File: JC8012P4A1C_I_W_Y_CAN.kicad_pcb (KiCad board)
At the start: 2 copper layers, 0 parts

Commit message: Add TBC power output, mounting holes and board outline
Schematic:
- TBC_PWR_out on D-Sub pin 8 like the Mueller-Elektronik BASIC-Terminal
  (some harnesses do not start without powered terminators):
  VIN_PROT -> SS16 Schottky (no back-feed) -> PTC 0.14 A -> J1 pin 6
- TBC_GND (D-Sub pin 3) to GND via R8 0R, DNP by default to stay
  compatible; fit R8 only if a harness needs the TBC_GND return
- Mounting holes H1-H4, M2, 2.2 mm (ISO 273 medium)
- Labels oriented away from pins, overlapping parts moved apart
  (netlist unchanged)

Board:
- Footprints imported from schematic (not placed yet)
- Outline 66 x 54 mm (provisional), holes on 58 x 46 mm grid,
  4 mm from the edge

Co-Authored-By: Claude Opus 5.5 <noreply@anthropic.com>
Claude-Session: https://claude.ai/code/session_014h8cGi8SRWthYdGFH1Qgzz
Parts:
- added C1: 47n, Capacitor_SMD:C_0603_1608Metric, F.Cu at (0.00, 0.00)
- added C2, C3: 100n, Capacitor_SMD:C_0603_1608Metric, F.Cu at (0.00, 0.00)
- added C4: 10u/50V, Capacitor_SMD:C_1210_3225Metric, F.Cu at (0.00, 0.00)
- added C5: 100u/10V, Capacitor_SMD:C_1210_3225Metric, F.Cu at (0.00, 0.00)
- added C6, C7: 22n, Capacitor_SMD:C_0603_1608Metric, F.Cu at (0.00, 0.00)
- added D1: 824094024, JC8012P4A1C_CAN:D_Wurth_WE-TVS-SOT23-3L, F.Cu at (0.00, 0.00)
- added D2: 824551241, JC8012P4A1C_CAN:D_Wurth_WE-TVSP-DO214-AB-3000W_BI, F.Cu at (0.00, 0.00)
- added D3: 15V, Diode_SMD:D_SOD-123, F.Cu at (0.00, 0.00)
- added D4: SS16, Diode_SMD:D_SMA, F.Cu at (0.00, 0.00)
- added F1: 1A slow, Fuse:Fuse_1206_3216Metric, F.Cu at (0.00, 0.00)
- added F2: PTC 0.14A/60V, Fuse:Fuse_1812_4532Metric, F.Cu at (0.00, 0.00)
- added H1: M2, MountingHole:MountingHole_2.2mm_M2, F.Cu at (104.0, 104.0)
- added H2: M2, MountingHole:MountingHole_2.2mm_M2, F.Cu at (162.0, 104.0)
- added H3: M2, MountingHole:MountingHole_2.2mm_M2, F.Cu at (104.0, 150.0)
- added H4: M2, MountingHole:MountingHole_2.2mm_M2, F.Cu at (162.0, 150.0)
- added J1: 61201022921, JC8012P4A1C_CAN:J_Wurth_WR-BHD_61201022921, F.Cu at (0.00, 0.00)
- added J2: 68711414522, JC8012P4A1C_CAN:J_Wurth_WR-FPC_68711414522, F.Cu at (0.00, 0.00)
- added J3: 653104131822, JC8012P4A1C_CAN:J_Wurth_WR-WTB_653104131822, F.Cu at (0.00, 0.00)
- added Q1: DMP6050SSD, Package_SO:SOIC-8_3.9x4.9mm_P1.27mm, F.Cu at (0.00, 0.00)
- added R1, R2: 750, Resistor_SMD:R_0603_1608Metric, F.Cu at (0.00, 0.00)
- added R3: 10k, Resistor_SMD:R_0603_1608Metric, F.Cu at (0.00, 0.00)
- added R4, R5: 100k, Resistor_SMD:R_0603_1608Metric, F.Cu at (0.00, 0.00)
- added R6: 5k62, Resistor_SMD:R_0603_1608Metric, F.Cu at (0.00, 0.00)
- added R7: 1k07, Resistor_SMD:R_0603_1608Metric, F.Cu at (0.00, 0.00)
- added R8: 0R DNP, Resistor_SMD:R_0603_1608Metric, F.Cu at (0.00, 0.00)
- added U1: TLE9250VSJ, Package_SO:SOIC-8_3.9x4.9mm_P1.27mm, F.Cu at (0.00, 0.00)
- added U2: 171030601, JC8012P4A1C_CAN:U_Wurth_WPME-VDRM-TO263-7EP, F.Cu at (0.00, 0.00)
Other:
- board outline added: 66 x 54 mm

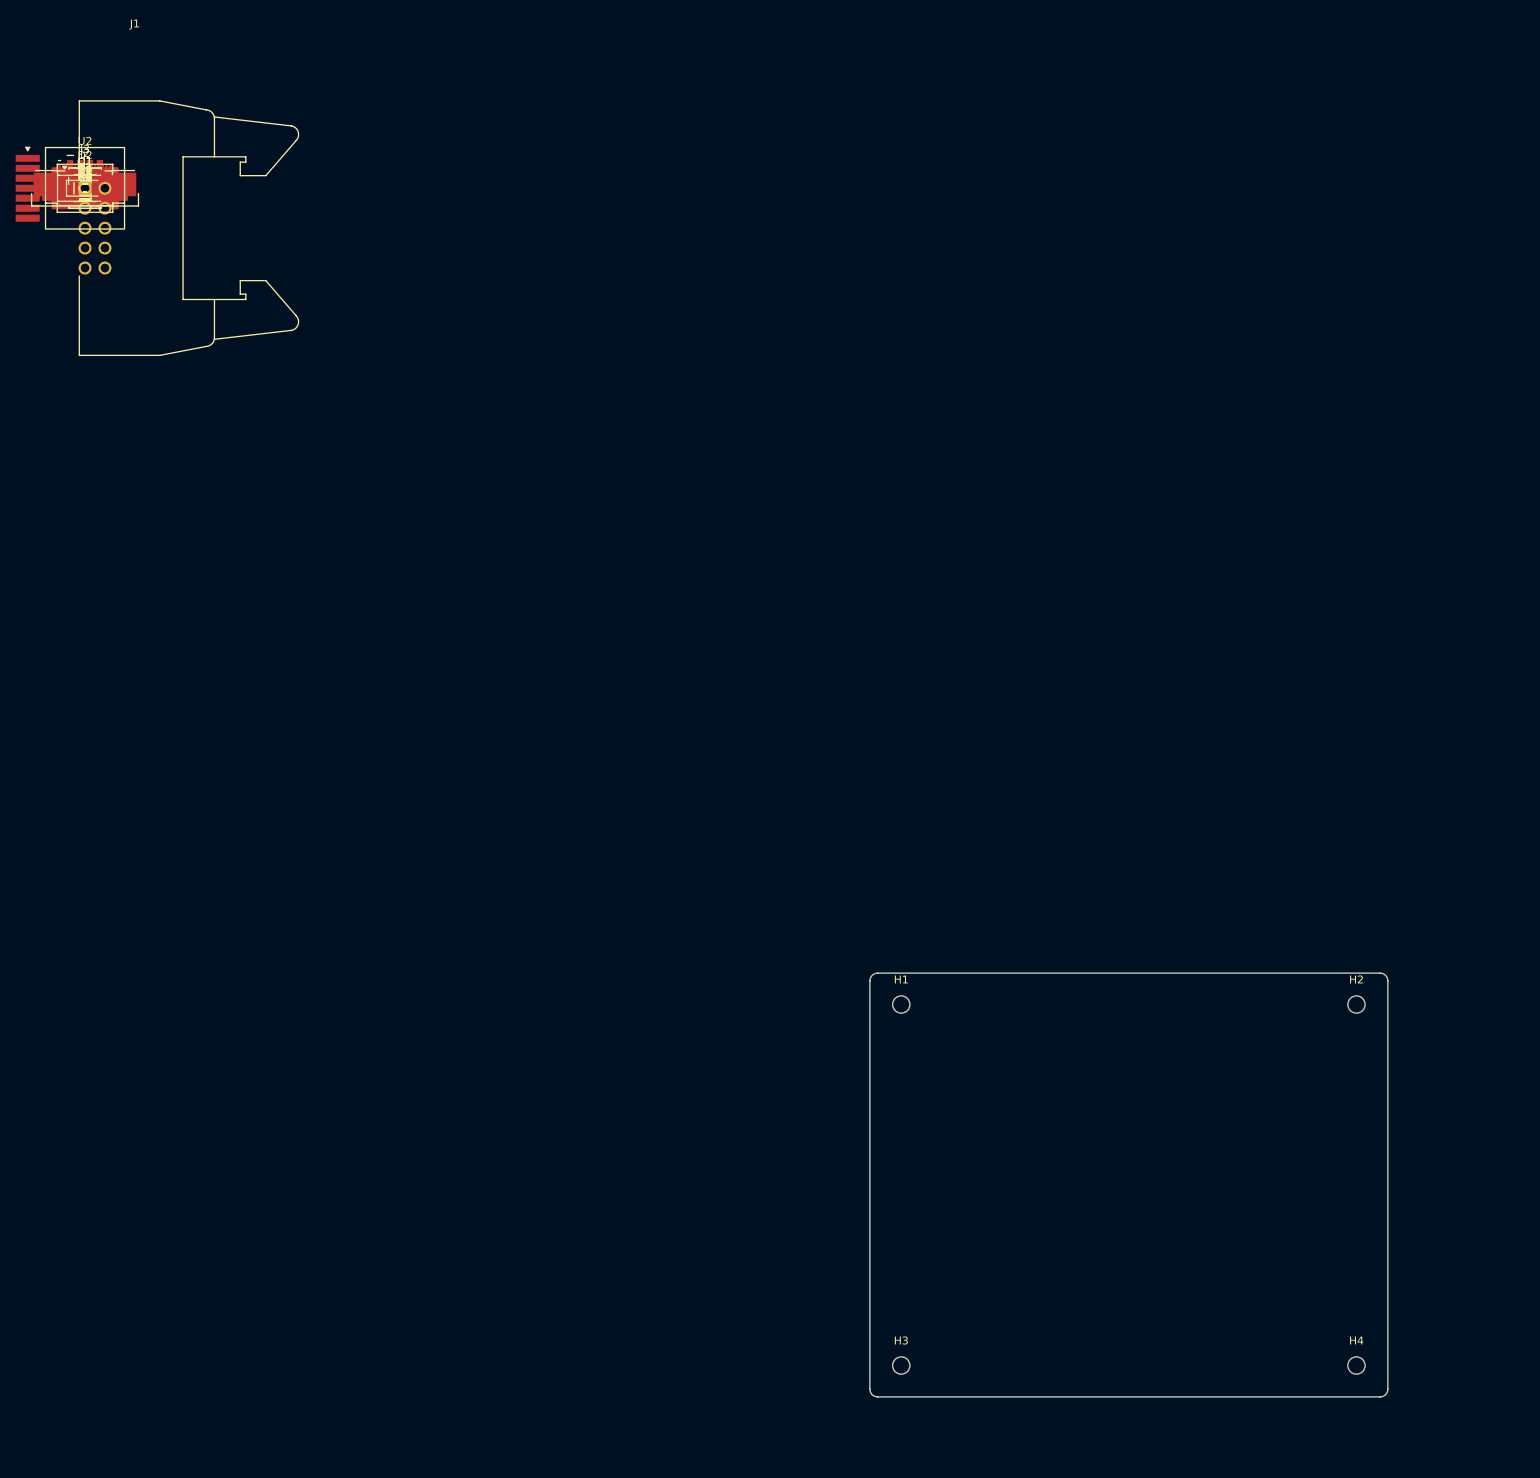
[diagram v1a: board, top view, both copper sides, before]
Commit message: Plate mounting holes to GND, fix PCB footprint links, add README
- H1-H4: MountingHole_Pad symbol, footprint MountingHole_2.2mm_M2_Pad_Via
  connected to GND (ground via the brass standoffs to the display
  board); excluded from BOM and position files
- PCB re-imported with KiCad "Update PCB from Schematic" (F8):
  footprints now linked to their symbols, net names /GND etc.,
  R8 marked DNP. The earlier import via KiCAD-MCP-Server created
  unlinked footprints.
- README: connectors, D-Sub 9 / J1 pinout, FPC3 pinout, termination,
  TBC power output and R8 (DNP by default, fit 0R if a harness needs
  the TBC_GND return), power section

Co-Authored-By: Claude Opus 5.5 <noreply@anthropic.com>
Claude-Session: https://claude.ai/code/session_014h8cGi8SRWthYdGFH1Qgzz
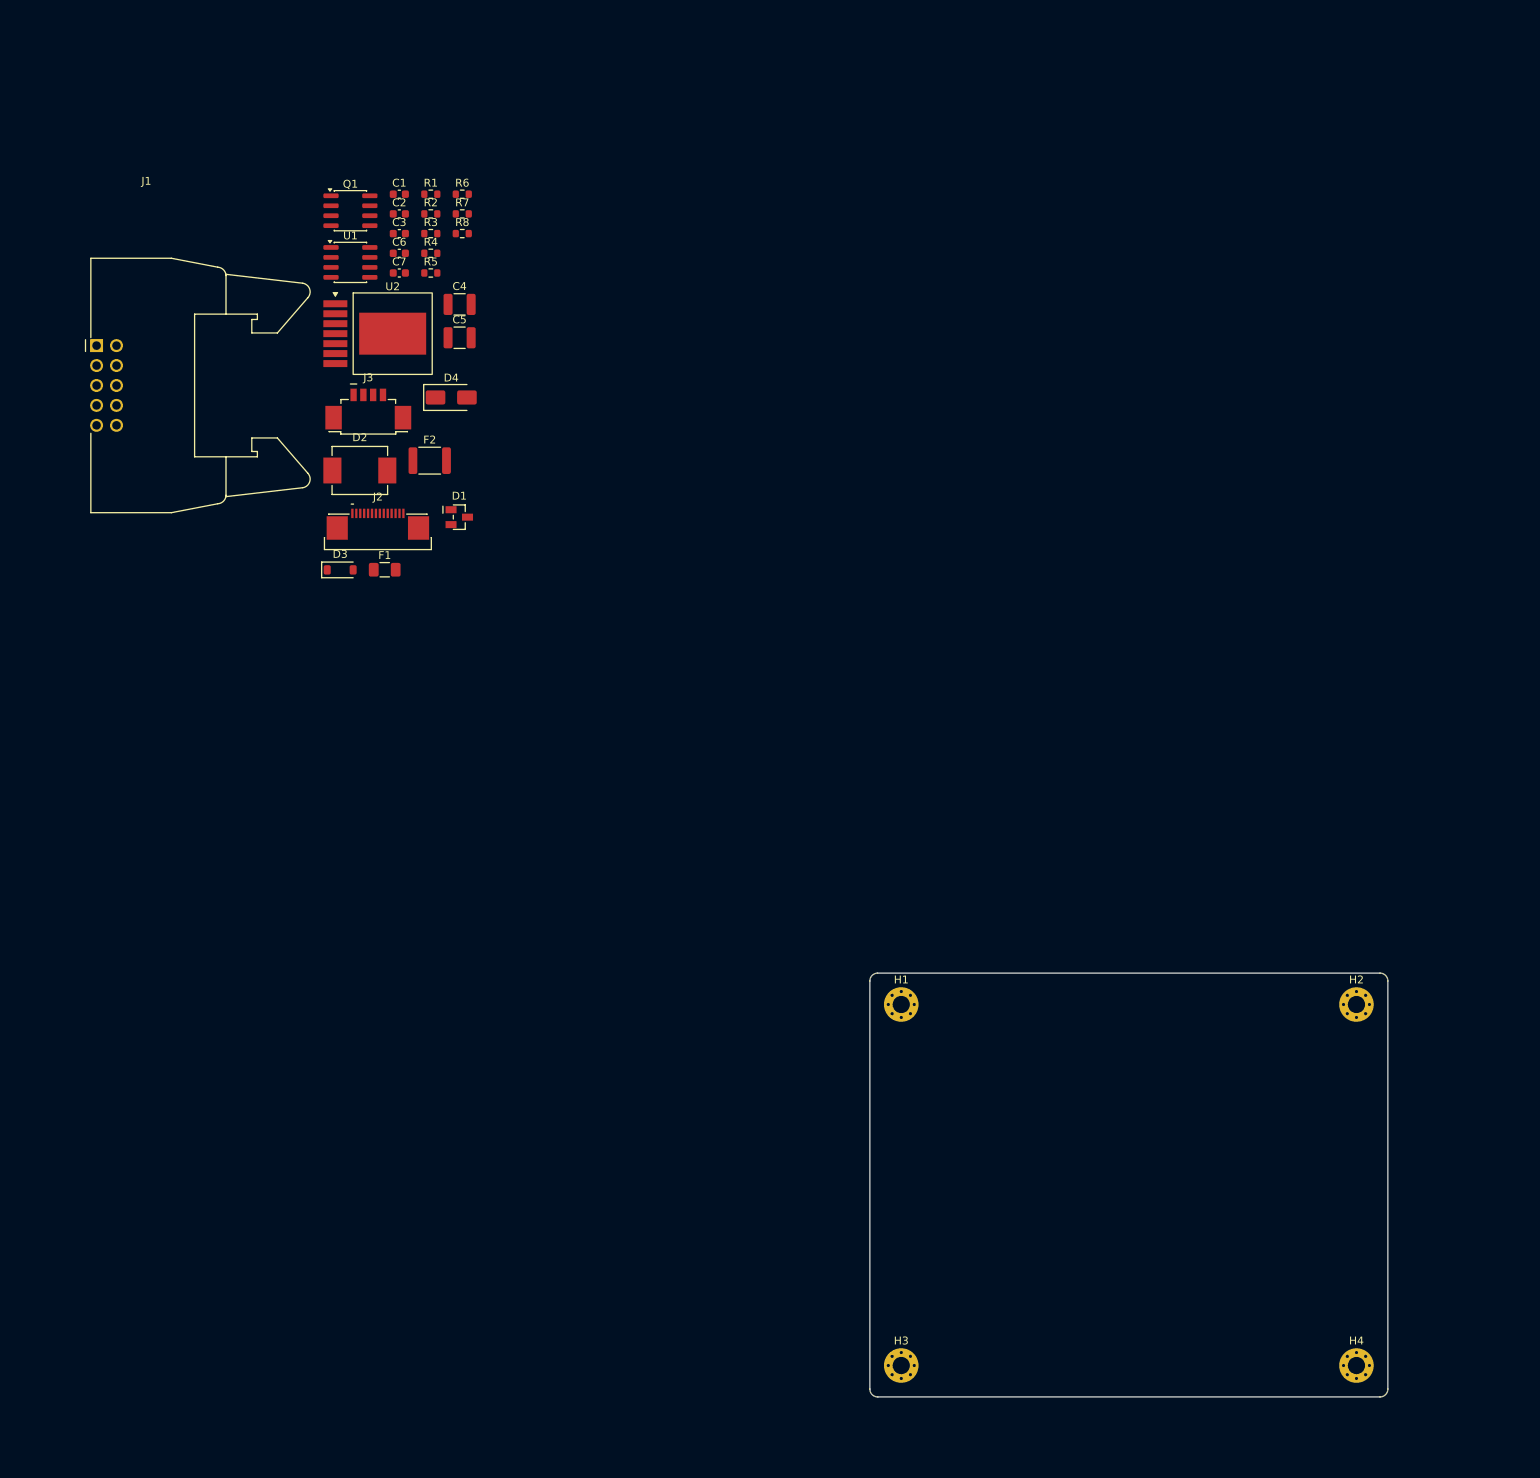
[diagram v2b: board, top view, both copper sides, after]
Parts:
- H1, H2, H3, H4: footprint MountingHole:MountingHole_2.2mm_M2 -> MountingHole:MountingHole_2.2mm_M2_Pad_Via
- moved D1 63.5 mm to (47.7, 41.9)
- moved F1 61.8 mm to (38.2, 48.6)
- moved D3 58.5 mm to (32.5, 48.6)
- moved J2 57.5 mm to (37.3, 43.8)
- moved F2 56.0 mm to (43.9, 34.7)
- moved D4 53.7 mm to (46.7, 26.7)
- moved C5 51.4 mm to (47.7, 19.0)
- moved D2 50.2 mm to (35.0, 36.0)
- moved C4 50.0 mm to (47.7, 14.8)
- moved R8 48.4 mm to (48.1, 5.78)
- moved R7 48.2 mm to (48.1, 3.27)
- moved R6 48.1 mm to (48.1, 0.76)
- moved J3 46.4 mm to (36.1, 29.1)
- moved R5 45.4 mm to (44.1, 10.8)
- moved R4 44.8 mm to (44.1, 8.29)
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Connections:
- net +3V3 renamed /+3V3
- net +5V renamed /+5V
- net BUCK_FB renamed /BUCK_FB
- net BUCK_RON renamed /BUCK_RON
- net BUCK_SS renamed /BUCK_SS
- net CAN_H renamed /CAN_H
- net CAN_L renamed /CAN_L
- net CAN_NEN renamed /CAN_NEN
- net CAN_RXD renamed /CAN_RXD
- net CAN_SPLIT renamed /CAN_SPLIT
- net CAN_TXD renamed /CAN_TXD
- net ECU_PWR renamed /ECU_PWR
- net ECU_PWR_IN renamed /ECU_PWR_IN
- net PFET_G renamed /PFET_G
- net TBC_GND renamed /TBC_GND
- net TBC_PWR_OUT renamed /TBC_PWR_OUT
- net VIN_PROT renamed /VIN_PROT
- C1 pad 2: GND -> /GND
- C2 pad 2: GND -> /GND
- C3 pad 2: GND -> /GND
- C4 pad 2: GND -> /GND
- C5 pad 2: GND -> /GND
- C6 pad 2: GND -> /GND
- D1 pad 3: GND -> /GND
- D2 pad 2: GND -> /GND
- J1 pad 10: (no net) -> unconnected-(J1-Pad10)
- J1 pad 2: GND -> /GND
- J1 pad 9: (no net) -> unconnected-(J1-Pad9)
- J2 pad 1: GND -> /GND
- J2 pad 10: (no net) -> unconnected-(J2-Pad10)
- J2 pad 11: (no net) -> unconnected-(J2-Pad11)
- J2 pad 12: (no net) -> unconnected-(J2-Pad12)
- J2 pad 2: GND -> /GND
- J2 pad 3: (no net) -> unconnected-(J2-Pad3)
- J2 pad 4: (no net) -> unconnected-(J2-Pad4)
- J2 pad 5: (no net) -> unconnected-(J2-Pad5)
- J2 pad 6: (no net) -> unconnected-(J2-Pad6)
- J2 pad Z1: GND -> /GND
- J2 pad Z2: GND -> /GND
- J3 pad 2: (no net) -> unconnected-(J3-Pad2)
- J3 pad 3: (no net) -> unconnected-(J3-Pad3)
- J3 pad 4: GND -> /GND
- R3 pad 2: GND -> /GND
- R4 pad 2: GND -> /GND
- R7 pad 2: GND -> /GND
- R8 pad 2: GND -> /GND
- U1 pad 2: GND -> /GND
- U2 pad 3: (no net) -> unconnected-(U2-EN-Pad3)
- U2 pad 4: GND -> /GND
- U2 pad EP: GND -> /GND

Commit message: Board outline with notches, place FPC connector J2
- Outline 66 x 54 mm, all corners R4: outer corners centred on the
  mounting holes, two notches (8 mm deep) for parts of the display
  board below: 100 uF electrolytic next to S4 (right edge) and the
  CR1220 RTC holder (bottom edge). Notch positions estimated from a
  photo, to be verified with a caliper.
- J2 rotated 180 deg like FPC3 (opening towards the top edge, pin 1 on
  the right), x aligned with FPC3, 20 mm from the edge for a 50 mm FFC
- README: FFC must be type B (opposite side contacts) because of the
  single 180 deg turn; pin 1 connects to pin 1

Co-Authored-By: Claude Opus 5.5 <noreply@anthropic.com>
Claude-Session: https://claude.ai/code/session_014h8cGi8SRWthYdGFH1Qgzz
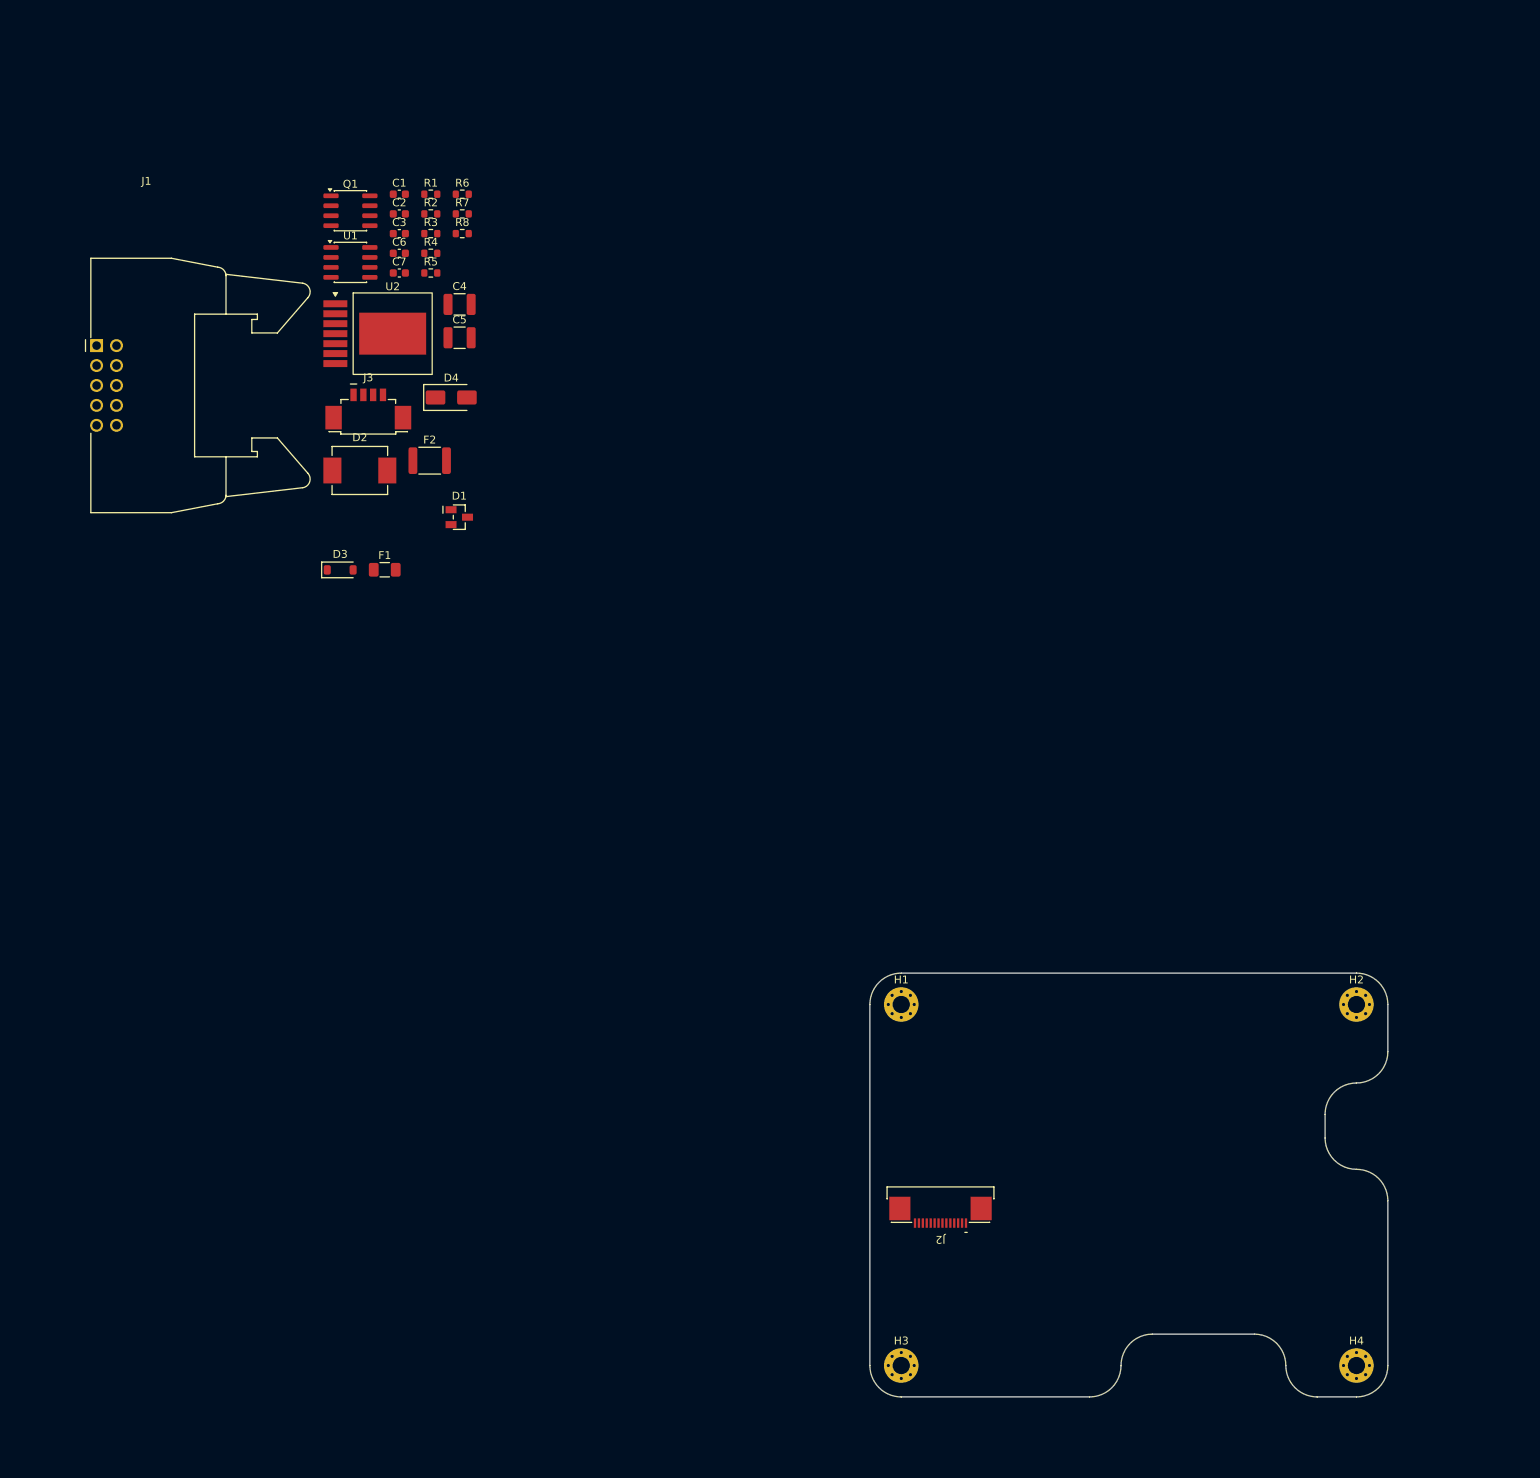
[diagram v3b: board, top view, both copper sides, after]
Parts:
- moved J2 111.7 mm to (109.0, 129.5), turned to 180 degrees
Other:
- outline, holes or cut-outs redrawn
